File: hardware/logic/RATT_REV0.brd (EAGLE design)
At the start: 127 x 76.2 mm, 134 parts, among them IC1 TLP292-4, IC13 MCP73832, IC16 PCA9539PW, IC2 CPC1002N, IC200 TPS2115AIPWRQ1, IC3 CPC1002N, IC300 MAX98357, IC4 CPC1002N, IC5 CPC1002N, IC500 AP2112K-3.3V, J1 4P-2.0, J100 PHOENIX1803426, J2 4P-2.0, J4 4P-2.0, J5 F-1X04-SIP-100-40, J6 4P-2.0, J7 PHOENIX1803484, J8 PHOENIX1803484, J87 RPI-ZERO, Q5 2N7002

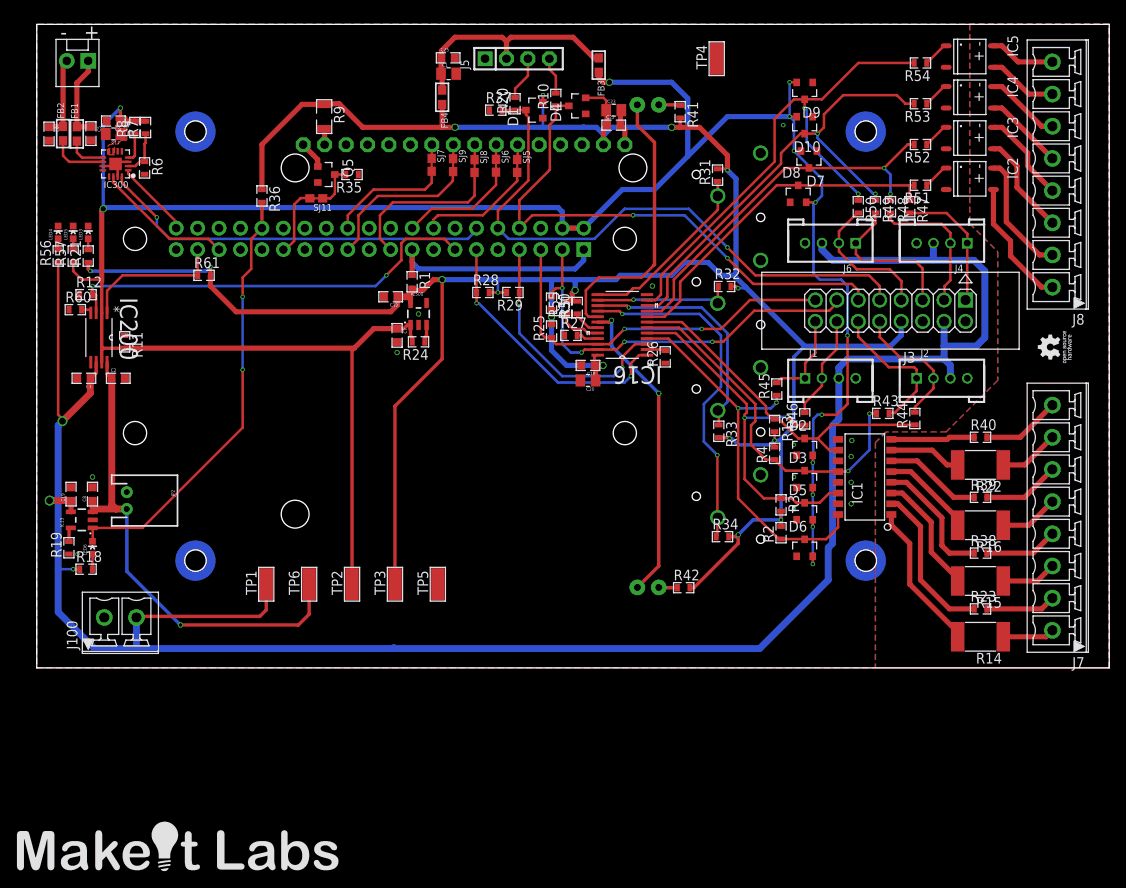
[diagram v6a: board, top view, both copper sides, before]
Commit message: Silkscreen
RefDes adjusted and normalized, text added, parts renumbered
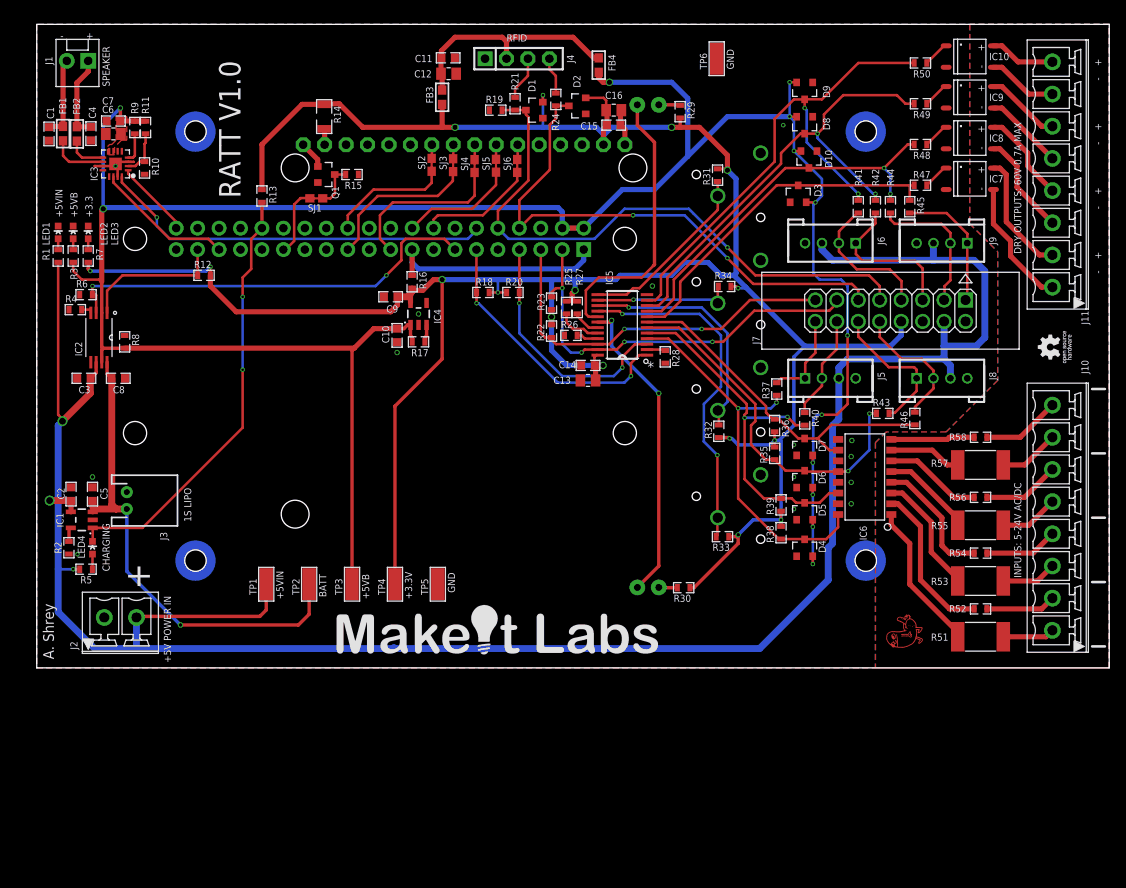
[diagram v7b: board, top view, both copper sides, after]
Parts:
- removed C17: 10uF, MakeItLabs:0805-CAP
- removed C19: 4.7uF, MakeItLabs:0603-CAP
- removed IC13: MCP73832, MakeItLabs:SOT23-5
- removed IC16: PCA9539PW, MakeItLabs:SOP65P640X120-24N
- removed IC200: TPS2115AIPWRQ1, MakeItLabs:SOP65P640X120-8N
- removed IC300: MAX98357, MakeItLabs:QFN16_3MM
- removed IC500: AP2112K-3.3V, MakeItLabs:SOT23-5
- removed J87: RPI-ZERO, MakeItLabs:RASPBERRYPI_BASTELSTUBE_V13_RASPI_BOARD_B+_FULL
- removed JP2: LiPo, MakeItLabs:JST-2-PTH
- removed JP4: (no value), MakeItLabs:MOLEX-1X2
- removed LED5, LED6: RED, MakeItLabs:LED-0603
- removed R60: 1k, MakeItLabs:0603-RES
- removed R61: 10k, MakeItLabs:0603-RES
- added C12: 10uF, MakeItLabs:0805-CAP
- added C4: 220pF, MakeItLabs:0603-CAP
- added IC10, IC7, IC8, IC9: CPC1002N, MakeItLabs:CPC1002N
- added IC6: TLP292-4, MakeItLabs:SO-16
- added J10, J11: PHOENIX1803484, MakeItLabs:1803484
- added J9: 4P-2.0, MakeItLabs:HW4-2.0
- added LED100, LED101: (no value), MakeItLabs:LED5MM
- added R17: 1k, MakeItLabs:0603-RES
- added R58: 0R, MakeItLabs:0603-RES
- C1: value 10uF -> 220pF; device MakeItLabs:0805-CAP -> MakeItLabs:0603-CAP
- C10: value 2.2uF -> 1.0uF
- C2: value 0.1uF -> 4.7uF
- C5: value 220pF -> 4.7uF
- C6: value 220pF -> 10uF; device MakeItLabs:0603-CAP -> MakeItLabs:0805-CAP
- C7: value 1.0uF -> 0.1uF
- C8: value 4.7uF -> 0.1uF
- C9: value 0.1uF -> 2.2uF
- IC1: value TLP292-4 -> MCP73832; device MakeItLabs:SO-16 -> MakeItLabs:SOT23-5
- IC2: value CPC1002N -> TPS2115AIPWRQ1; device MakeItLabs:CPC1002N -> MakeItLabs:SOP65P640X120-8N
- IC3: value CPC1002N -> MAX98357; device MakeItLabs:CPC1002N -> MakeItLabs:QFN16_3MM
- IC4: value CPC1002N -> AP2112K-3.3V; device MakeItLabs:CPC1002N -> MakeItLabs:SOT23-5
- IC5: value CPC1002N -> PCA9539PW; device MakeItLabs:CPC1002N -> MakeItLabs:SOP65P640X120-24N
- J1: value 4P-2.0 -> (none); device MakeItLabs:HW4-2.0 -> MakeItLabs:MOLEX-1X2
- J100: value PHOENIX1803426 -> RPI-ZERO; device MakeItLabs:1803426 -> MakeItLabs:RASPBERRYPI_BASTELSTUBE_V13_RASPI_BOARD_B+_FULL
- J2: value 4P-2.0 -> PHOENIX1803426; device MakeItLabs:HW4-2.0 -> MakeItLabs:1803426
- J3: value (none) -> LiPo; device MakeItLabs:2X08_SHROUD -> MakeItLabs:JST-2-PTH
- J4: value 4P-2.0 -> F-1X04-SIP-100-40; device MakeItLabs:HW4-2.0 -> MakeItLabs:SIP-100-04-40
- J5: value F-1X04-SIP-100-40 -> 4P-2.0; device MakeItLabs:SIP-100-04-40 -> MakeItLabs:HW4-2.0
- J7: value PHOENIX1803484 -> (none); device MakeItLabs:1803484 -> MakeItLabs:2X08_SHROUD
- J8: value PHOENIX1803484 -> 4P-2.0; device MakeItLabs:1803484 -> MakeItLabs:HW4-2.0
- LED1, LED2: value (none) -> RED; device MakeItLabs:LED5MM -> MakeItLabs:LED-0603
- R1: value 0R -> 1K
- R10: value 100R -> 100K
- R11: value 10k -> 100K
- R13, R3, R5: value 10K -> 1K
- R14: value 680R -> 10R; device MakeItLabs:2512-RES -> MakeItLabs:1206-RES
- R15, R22: value 680R -> 10K; device MakeItLabs:2512-RES -> MakeItLabs:0603-RES
- R16: value 680R -> 0R; device MakeItLabs:2512-RES -> MakeItLabs:0603-RES
- R18, R36: value 1K -> 10K
- R19: value 2.0k -> 1.5K
- R2: value 10K -> 2.0k
- R20: value 750R -> 10K
- R21: value 1K -> 750R
- R23, R38, R39: value 0R -> 10K
- R24: value 1k -> 100R
- R29, R30: value 10K -> 680R
- R37: value 1.5K -> 100R
- R4: value 10K -> 1k
- R40: value 0R -> 100R
- R41, R42: value 680R -> 100R
- R47, R48, R49, R50: value 100R -> 680R
- R51, R53: device MakeItLabs:0603-RES -> MakeItLabs:2512-RES
- R52, R54: value 680R -> 0R
- R55: value 10K -> 680R; device MakeItLabs:0603-RES -> MakeItLabs:2512-RES
- R56: value 1K -> 0R
- R57: value 1K -> 680R; device MakeItLabs:0603-RES -> MakeItLabs:2512-RES
- R6: value 100K -> 10k
- R7: value 100K -> 1K
- R8: value 680K -> 10k
- R9: value 10R -> 680K; device MakeItLabs:1206-RES -> MakeItLabs:0603-RES
- TP2: value 5VB -> BATT
- TP3: value 3.3V -> 5VB
- TP4: value GND -> 3.3V
- TP6: value BATT -> GND
- moved R56 112.9 mm to (111.8, 20.2), turned to 0 degrees
- moved R57 110.3 mm to (111.8, 24.0), turned to 180 degrees
- moved IC2 104.8 mm to (7.37, 39.1)
- moved J2 101.5 mm to (9.91, 5.33)
- moved IC3 101.2 mm to (9.33, 59.7), turned to 180 degrees
- moved R14 99.2 mm to (34.0, 65.3), turned to 270 degrees
- moved J1 95.6 mm to (6.10, 71.9), turned to 180 degrees
- moved J3 93.2 mm to (10.7, 19.8), turned to 270 degrees
- moved IC1 92.8 mm to (5.33, 17.5)
- moved R3 88.8 mm to (4.32, 48.8), turned to 90 degrees
- moved R15 88.6 mm to (37.3, 58.4)
- moved R4 84.5 mm to (4.57, 42.4), turned to 0 degrees
- moved R2 84.3 mm to (3.81, 14.2)
- moved LED2 80.0 mm to (4.32, 51.6), flipped to the top
- moved TP6 78.8 mm to (80.5, 72.1)
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- renumbered C18 to C14, C20 to C13, C22 to C15, C23 to C16, C25 to C11, LCD3 to LCD100, Q5 to Q1, SJ11 to SJ1, SJ7 to SJ2, SJ8 to SJ4, SJ9 to SJ3, SW0 to SW103, SW1 to SW102, SW2 to SW101, SW3 to SW100
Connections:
- net !BUTTON0: now also IC5.13; no longer IC16.13
- net !BUTTON1: now also IC5.14, R34.1; no longer IC16.14, R32.1
- net !BUTTON2: now also IC5.15, R32.1; no longer IC16.15, R33.1
- net !BUTTON3: now also IC5.16, R33.1; no longer IC16.16, R34.1
- net !I/O_IRQ: now also IC5.1, J100.11, R18.1; no longer IC16.1, J87.11, R28.1
- net !I/O_RESET: now also IC5.3, J100.7, R20.1; no longer IC16.3, J87.7, R29.1
- net !PWR_LOSS: now also IC2.1, J100.37, R12.1; no longer IC200.1, J87.37, R61.1
- net +3.3V: now also C9.1, D2.2, FB3.2, IC4.5, IC5.24, J7.8, R12.2, R13.1, R14.1, R16.2, R18.2, R20.2, R22.2, R23.2, R27.2, R35.2, R36.2, R38.2, R39.2, R7.1, TP4.1; no longer C10.1, D4.2, FB4.2, IC16.24, IC500.5, J3.8, R1.2, R13.2, R2.2, R21.1, R28.2, R3.2, R36.1, R4.2, R41.2, R42.2, R5.2, R55.2, R61.2, R9.1, TP3.1
- net +5VB: now also C10.1, C6.1, D4.2, FB4.2, IC2.2, IC2.7, IC3.7, IC3.8, IC4.1, J100.2, J100.4, R17.2, R3.1, R9.2, TP3.1; no longer C17.1, C9.1, D2.2, FB3.2, IC200.2, IC200.7, IC300.7, IC300.8, IC500.1, J87.2, J87.4, R24.2, R57.1, R7.2, TP2.1
- net +5VIN: now also C2.1, IC1.4, IC2.6, J2.2, J5.3, J7.4, J8.3, J9.3, R1.1, R5.1; no longer C19.1, IC13.4, IC200.6, J1.3, J100.2, J2.3, J3.4, J4.3, R18.1, R56.1
- net 3V3: now also J100.1, J100.17, R16.1; no longer J87.1, J87.17, R1.1
- net 5V_RFID_TX: now also J4.3, R21.2; no longer J5.3, R20.2
- net CHARGE_STATUS: now also IC1.1, J100.32, LED4.C, R13.2; no longer IC13.1, J87.32, LED6.C, R36.2
- net GND: now also C12.2, C4.2, IC1.2, IC10.2, IC2.5, IC3.11, IC3.15, IC3.3, IC3.THERMAL, IC5.12, IC6.11, IC6.13, IC6.15, IC6.9, IC7.2, IC8.2, IC9.2, J100.14, J100.20, J100.25, J100.30, J100.34, J100.39, J100.6, J100.9, J2.1, J3.1, J4.1, J5.4, J7.2, J7.6, J8.4, J9.4, LED1.C, LED2.C, R10.2, R15.1, R2.1, R28.1, R4.1, R6.1, R8.1, TP6.1; no longer C17.2, C19.2, IC1.11, IC1.13, IC1.15, IC1.9, IC13.2, IC16.12, IC2.2, IC200.5, IC3.2, IC300.11, IC300.15, IC300.3, IC300.THERMAL, IC5.2, IC500.2, J1.4, J100.1, J2.4, J3.2, J3.6, J4.4, J5.1, J87.14, J87.20, J87.25, J87.30, J87.34, J87.39, J87.6, J87.9, JP2.1, LED4.C, LED5.C, R11.1, R12.1, R27.1, R35.1, R37.1, R6.2, R60.1, TP4.1
- net I2C_SCL: now also IC5.22, J100.5, J7.15, R22.1; no longer IC16.22, J3.15, J87.5, R25.1
- net I2C_SDA: now also IC5.23, J100.3, J7.13, R23.1; no longer IC16.23, J3.13, J87.3, R30.1
- net I2S_BCK: now also IC3.16, J100.12; no longer IC300.16, J87.12
- net I2S_DOUT: now also IC3.1, J100.40; no longer IC300.1, J87.40
- net I2S_WS/LRCLK: now also IC3.14, J100.35; no longer IC300.14, J87.35
- net IN0: now also D4.3, IC5.4, IC6.16, R37.1, R38.1; no longer D6.3, IC1.16, IC16.4, R2.1, R45.1
- net IN0P: now also J5.1, J7.16, R37.2; no longer J1.1, J3.16, R45.2
- net IN1: now also IC5.5, IC6.14, R39.1, R40.1; no longer IC1.14, IC16.5, R3.1, R46.1
- net IN1P: now also J5.2, J7.14, R40.2; no longer J1.2, J3.14, R46.2
- net IN2: now also D6.3, IC5.6, IC6.12, R35.1; no longer D3.3, IC1.12, IC16.6, R4.1
- net IN2P: now also J7.12, J8.1; no longer J2.1, J3.12
- net IN3: now also D7.3, IC5.7, IC6.10, R36.1, R46.1; no longer D2.3, IC1.10, IC16.7, R13.1, R44.1
- net IN3P: now also J7.10, J8.2, R46.2; no longer J2.2, J3.10, R44.2
- net LCD_BACKLIGHT: now also J100.29; no longer J87.29
- net LCD_CS: now also J100.24; no longer J87.24
- net LCD_D/C: now also J100.18, SJ5.2; no longer J87.18, SJ6.2
- net LCD_MISO: now also J100.21; no longer J87.21
- net LCD_MOSI: now also J100.19; no longer J87.19
- net LCD_RESET: now also J100.16, SJ6.2; no longer J87.16, SJ5.2
- net LCD_SCK: now also J100.23; no longer J87.23
- net LED0: now also IC5.17, LED101.K; no longer IC16.17, LED1.K
- net LED1: now also IC5.18, LED100.K; no longer IC16.18, LED2.K
- net N$1: now also IC3.2, R10.1, R11.1; no longer IC300.2, R6.1, R7.1
- net N$10: now also J4.4, R24.2; no longer J5.4, R10.2
- net N$11: now also R7.2; no longer R21.2
- net N$12: now also LED2.A, R3.2; no longer LED5.A, R57.2
- net N$13: now also IC5.19, R27.1; no longer IC16.19, R5.1
- net N$14: now also IC1.5, R2.2; no longer IC13.5, R19.2
- net N$15: now also IC6.2, R52.1; no longer IC1.2, R23.1
- net N$17: now also LED4.A, R5.2; no longer LED6.A, R18.2
- net N$18: now also IC4.3, R17.1; no longer IC500.3, R24.1
- net N$19: now also IC6.1, R51.2; no longer IC1.1, R14.2
- net N$2: now also FB2.1, IC3.9; no longer FB1.1, IC300.9
- net N$20: now also IC6.8, R58.1; no longer IC1.8, R40.1
- net N$21: now also IC5.21, R26.2; no longer IC16.21, R27.2
- net N$22: now also IC5.2, R28.2; no longer IC16.2, R26.2
- net N$23: now also IC6.7, R57.2; no longer IC1.7, R22.2
- net N$24: now also IC6.6, R56.1; no longer IC1.6, R39.1
- net N$25: now also IC6.5, R55.2; no longer IC1.5, R16.2
- net N$27: now also SJ6.1; no longer SJ5.1
- net N$28: now also SJ5.1; no longer SJ6.1
- net N$32: now also IC7.3, J11.1; no longer IC2.3, J8.1
- net N$33: now also R15.2; no longer R35.2
- net N$36: now also IC6.4, R54.1; no longer IC1.4, R38.1
- net N$37: now also IC2.4, R4.2; no longer IC200.4, R60.2
- net N$39: now also IC6.3, R53.2; no longer IC1.3, R15.2
- net N$4: now also FB1.1, IC3.10; no longer FB2.1, IC300.10
- net N$40: now also J10.4, R54.2; no longer J7.4, R38.2
- net N$41: now also J10.3, R53.1; no longer J7.3, R15.1
- net N$42: now also J10.2, R52.2; no longer J7.2, R23.2
- net N$43: now also J10.1, R51.1; no longer J7.1, R14.1
- net N$44: now also J10.5, R55.1; no longer J7.5, R16.1
- net N$45: now also J10.6, R56.2; no longer J7.6, R39.2
- net N$46: now also J10.7, R57.1; no longer J7.7, R22.1
- net N$47: now also J10.8, R58.2; no longer J7.8, R40.2
- net N$48: now also LED101.A, R29.1; no longer LED1.A, R41.1
- net N$49: now also LED100.A, R30.1; no longer LED2.A, R42.1
- net N$5: now also IC3.4, R9.1; no longer IC300.4, R8.1
- net N$50: now also LED1.A, R1.2; no longer LED4.A, R56.2
- net N$51: now also C12.1, J4.2; no longer C1.1, J5.2
- net N$58: now also IC7.1, R47.1; no longer IC2.1, R51.1
- net N$59: now also IC7.4, J11.2; no longer IC2.4, J8.2
- net N$6: now also C1.1, FB1.2, J1.2; no longer C6.1, FB2.2, JP4.2
- net N$60: now also IC10.3, J11.7; no longer IC5.3, J8.7
- net N$61: now also IC8.1, R48.1; no longer IC3.1, R52.1
- net N$62: now also IC10.4, J11.8; no longer IC5.4, J8.8
- net N$63: now also IC9.3, J11.5; no longer IC4.3, J8.5
- net N$64: now also IC9.4, J11.6; no longer IC4.4, J8.6
- net N$65: now also IC8.3, J11.3; no longer IC3.3, J8.3
- net N$66: now also IC8.4, J11.4; no longer IC3.4, J8.4
- net N$68: now also IC9.1, R49.1; no longer IC4.1, R53.1
- net N$69: now also IC10.1, R50.1; no longer IC5.1, R54.1
- net N$7: now also C4.1, FB2.2, J1.1; no longer C5.1, FB1.2, JP4.1
- net N$8: now also IC5.20, R25.1; no longer IC16.20, R55.1
- net N$9: now also R14.2; no longer R9.2
- net OUT0: now also D3.3, IC5.8, R45.1, R47.2; no longer D8.3, IC16.8, R47.1, R51.2
- net OUT0P: now also J7.1, J9.1, R45.2; no longer J3.1, J4.1, R47.2
- net OUT1: now also D10.3, IC5.9, R44.1, R48.2; no longer D7.3, IC16.9, R48.1, R52.2
- net OUT1P: now also J7.3, J9.2, R44.2; no longer J3.3, J4.2, R48.2
- net OUT2: now also D8.3, IC5.10, R42.1, R49.2; no longer D10.3, IC16.10, R49.1, R53.2
- net OUT2P: now also J7.5, R42.2; no longer J3.5, R49.2
- net OUT3: now also IC5.11, R41.1, R50.2; no longer IC16.11, R50.1, R54.2
- net OUT3P: now also J7.7, R41.2; no longer J3.7, R50.2
- net RFID_RX: now also D2.3, J100.8, J7.11, R24.1; no longer D4.3, J3.11, J87.8, R10.1
- net RFID_TX: now also J100.10, J7.9, R19.2, R21.1; no longer J3.9, J87.10, R20.1, R37.2
- net SHUTDOWN: now also IC2.3, J100.13, R6.2; no longer IC200.3, J87.13, R12.2
- net V_BATT: now also C5.1, IC1.3, IC2.8, J3.2, TP2.1; no longer C2.1, IC13.3, IC200.8, JP2.2, TP6.1
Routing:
- net GND: track 9.24 -> 11.1 mm, vias 13 -> 14
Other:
- board text added: "+3.3"
- board text added: "+3.3V"
- board text added: "+5V POWER IN"
- board text added: "+5VB"
- board text added: "+5VIN"
- board text added: "- +"
- board text added: "1S LIPO"
- board text added: "A. Shrey"
- board text added: "BATT"
- board text added: "CHARGING"
- board text added: "DRY OUTPUTS: 60V 0.7A MAX"
- board text added: "GND"
- board text added: "INPUTS: 5-24V AC/DC"
- board text added: "RATT V1.0"
- board text added: "RFID"
- board text added: "SPEAKER"
